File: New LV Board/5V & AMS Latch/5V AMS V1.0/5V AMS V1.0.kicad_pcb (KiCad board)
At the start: 2 copper layers, 46.4 x 64.5 mm, 19 parts, among them J2 B12B-PH-K-S, J4 691137710002, J6 PH1-20-UA, J9 PH1-20-UA, K1 AHES4291, SW1 Test Reset AMS, U1 LT1117-5.0

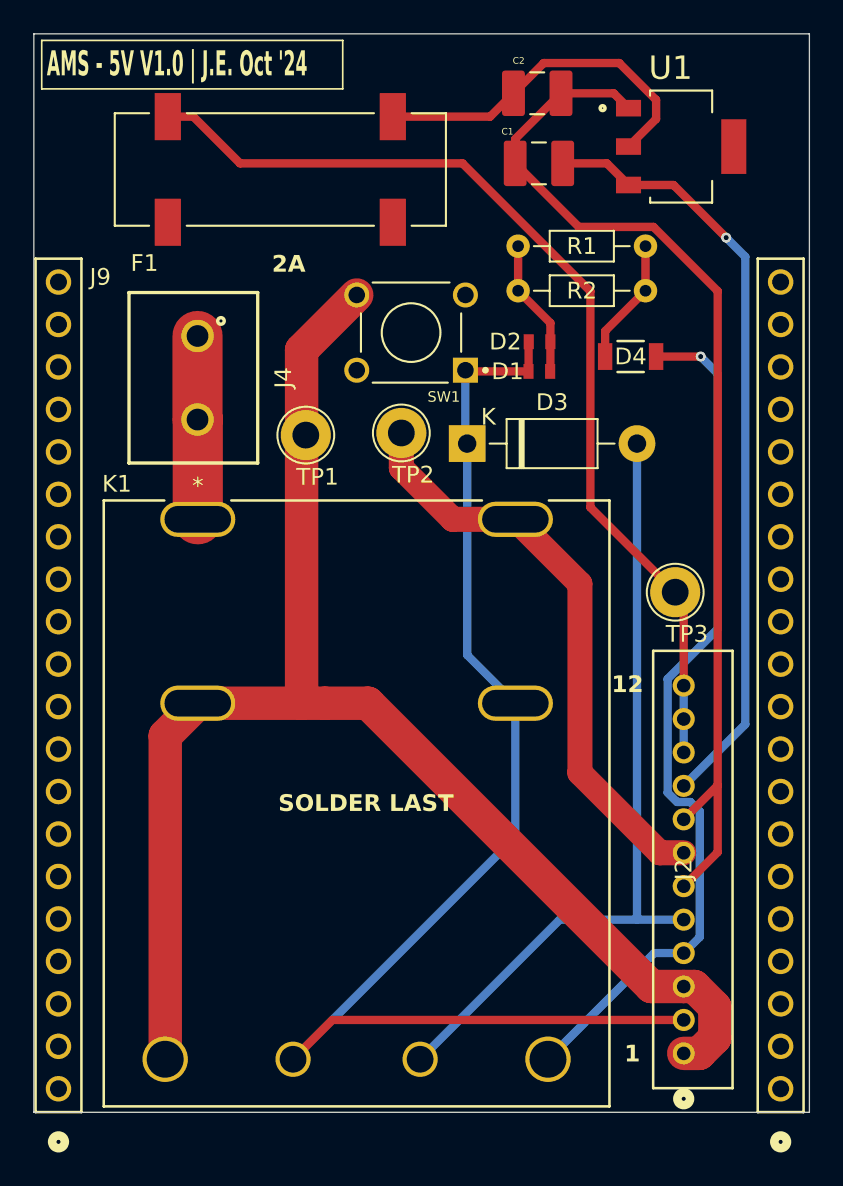
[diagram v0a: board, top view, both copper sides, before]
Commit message: getting dimensions correct for 5V AMS
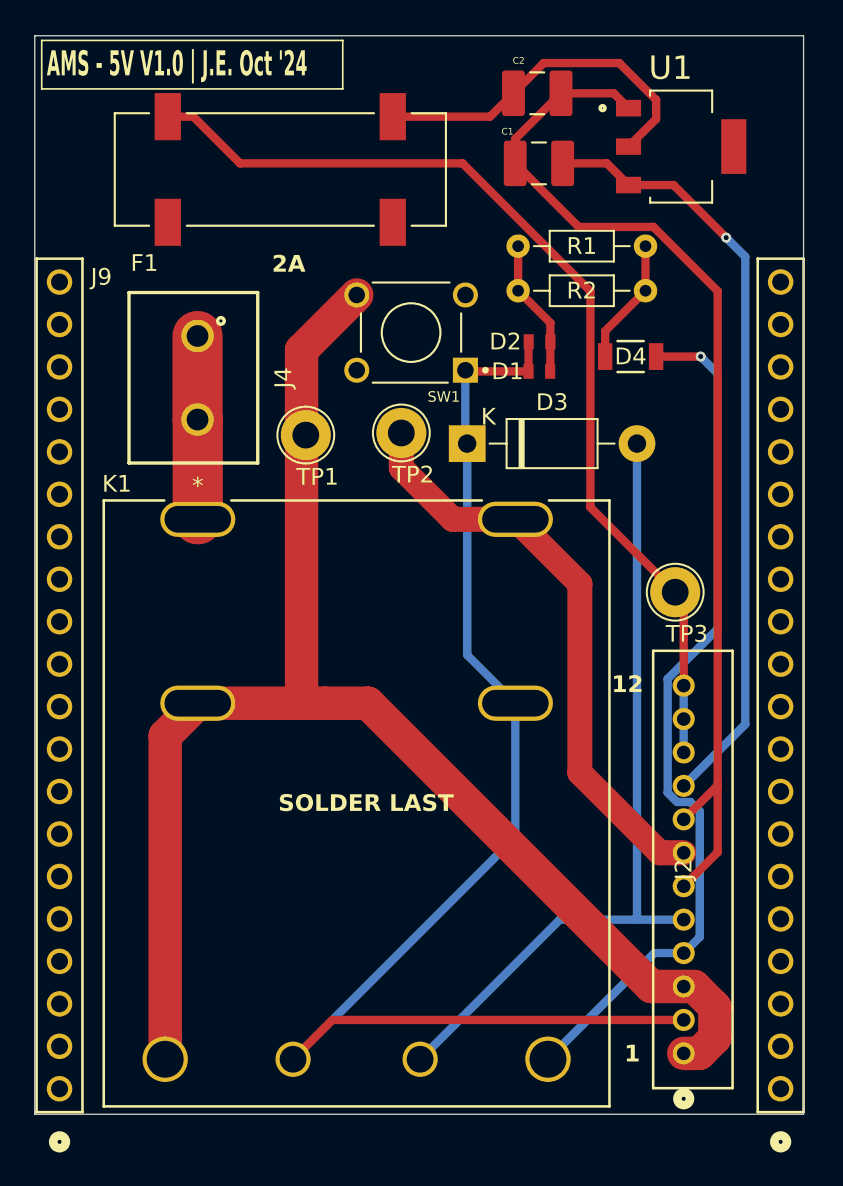
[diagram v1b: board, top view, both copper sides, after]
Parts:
- moved J9 0.06 mm to (59.9, 168.6)
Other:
- board size 46.4 x 64.5 mm -> 46 x 64.5 mm
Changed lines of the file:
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@@
 	(footprint "PH1-20-UA:CONN_PH1-20-UA_ADM"
 		(layer "F.Cu")
-		(at 59.881 168.643 90)
+		(at 59.944 168.643 90)
 		(tags "PH1-20-UA ")
 		(property "Reference" "J9"
@@
 	)
 	(gr_rect
-		(start 58.407 105.537)
-		(end 104.801 170.053)
+		(start 58.464 105.651)
+		(end 104.4516 170.167)
 		(stroke
 			(width 0.05)
@@
 		)
 	)
+	(dimension
+		(type orthogonal)
+		(layer "Dwgs.User")
+		(pts
+			(xy 104.4516 105.651) (xy 104.4516 170.167)
+		)
+		(height 5.2002)
+		(orientation 1)
+		(format
+			(prefix "")
+			(suffix "mm")
+			(units 3)
+			(units_format 0)
+			(precision 4)
+			(suppress_zeroes yes)
+		)
+		(style
+			(thickness 0.2)
+			(arrow_length 1.27)
+			(text_position_mode 0)
+			(arrow_direction outward)
+			(extension_height 0.58642)
+			(extension_offset 0.5)
+		)
+		(gr_text "64.516mm"
+			(at 107.8518 137.909 90)
+			(layer "Dwgs.User")
+			(effects
+				(font
+					(size 1.5 1.5)
+					(thickness 0.3)
+				)
+			)
+		)
+	)
+	(dimension
+		(type orthogonal)
+		(layer "Dwgs.User")
+		(pts
+			(xy 58.4708 169.418) (xy 104.4708 169.418)
+		)
+		(height 15.748)
+		(orientation 0)
+		(format
+			(prefix "")
+			(suffix "")
+			(units 3)
+			(units_format 1)
+			(precision 4)
+		)
+		(style
+			(thickness 0.05)
+			(arrow_length 1.27)
+			(text_position_mode 0)
+			(arrow_direction outward)
+			(extension_height 0.58642)
+			(extension_offset 0.5)
+			(keep_text_aligned yes)
+		)
+		(gr_text "46.0000 mm"
+			(at 81.4708 184.016 0)
+			(layer "Dwgs.User")
+			(effects
+				(font
+					(size 1 1)
+					(thickness 0.15)
+				)
+			)
+		)
+	)
+	(dimension
+		(type orthogonal)
+		(layer "Dwgs.User")
+		(pts
+			(xy 103.124 168.275) (xy 59.944 168.275)
+		)
+		(height 9.144)
+		(orientation 0)
+		(format
+			(prefix "")
+			(suffix "")
+			(units 3)
+			(units_format 1)
+			(precision 4)
+		)
+		(style
+			(thickness 0.05)
+			(arrow_length 1.27)
+			(text_position_mode 0)
+			(arrow_direction outward)
+			(extension_height 0.58642)
+			(extension_offset 0.5)
+			(keep_text_aligned yes)
+		)
+		(gr_text "43.1800 mm"
+			(at 81.534 176.269 0)
+			(layer "Dwgs.User")
+			(effects
+				(font
+					(size 1 1)
+					(thickness 0.15)
+				)
+			)
+		)
+	)

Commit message: PCB cleanup and retrace
PCB cleanup and retrace
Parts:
- removed K1: AHES4291, motorSports:AHES4_PAN
- removed TP1, TP2, TP3: TestPoint, TestPoint:TestPoint_Loop_D2.60mm_Drill1.6mm_Beaded
- added K2: A161CS12VDC.64, Footprints:RELAY_A161CS12VDC.64, F.Cu at (76.5, 140.9)
- added K3: A161CS12VDC.64, Footprints:RELAY_A161CS12VDC.64, F.Cu at (76.5, 150.0)
- added K4: A161CS12VDC.64, Footprints:RELAY_A161CS12VDC.64, F.Cu at (76.5, 159.1)
- J2: footprint MotorSports_KICad:CONN12_B12B-PH_JST -> Footprints:JST_B12B-PH-K-S
- moved F1 35.5 mm to (94.8, 141.8), turned to 90 degrees
- moved R1 34.3 mm to (86.0, 152.5), turned to 90 degrees
- moved D2 33.1 mm to (89.4, 157.0)
- moved D3 30.7 mm to (88.3, 160.5)
- moved D4 29.7 mm to (95.0, 154.5)
- moved D1 28.8 mm to (89.4, 154.5)
- moved R2 19.3 mm to (86.0, 140.1), turned to 90 degrees
- moved C2 18.0 mm to (86.6, 127.0)
- moved J2 14.8 mm to (82.5, 166.6), turned to 180 degrees
- moved U1 12.3 mm to (96.0, 124.5)
- moved C1 8.95 mm to (86.6, 122.0)
- moved SW1 6.72 mm to (78.8, 129.8)
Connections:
- D3 pad 2: Net-(D3-A) -> Net-(D1-K)
- J2 pad 5: Net-(D3-A) -> Net-(D1-K)
- SW1 pad 2: (no net) -> Net-(J2-Pad1)
- SW1 pad 4: Net-(J2-Pad1) -> (no net)
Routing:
- net Net-(J2-Pad1): track 90.4 -> 41.9 mm
- net Net-(D3-A): track 47.7 -> 0.00 mm
- net Net-(F1-Pad1_1): track 59.7 -> 23.8 mm
- net Net-(J2-Pad7): track 35.1 -> 4.92 mm
- net Net-(D4-K): track 7.60 -> 33.0 mm, vias 0 -> 1
- net Net-(J4-Pad1): track 11.0 -> 36.4 mm
- net Net-(D1-K): track 77.9 -> 73.4 mm
- net /GND: track 72.6 -> 68.3 mm
- net Net-(U1-VO): track 21.5 -> 24.6 mm, vias 0 -> 2
- net /Vs: track 46.4 -> 49.3 mm, vias 1 -> 0
- net Net-(D4-A): track 52.4 -> 52.2 mm, vias 1 -> 2
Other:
- board size 46 x 64.5 mm -> 46 x 51.5 mm
- board text added: "AMS - 5V V1.0 | H.R. Nov 13' 2025"
- board text removed: "AMS - 5V V1.0 | J.E. Oct '24"

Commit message: cleaned up schematics
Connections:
- D2 pad 1: Net-(D1-K) -> Net-(D2-K)
- D3 pad 1: Net-(D1-K) -> Net-(D2-K)
- D3 pad 2: Net-(D1-K) -> Net-(D3-A)
- J2 pad 2: Net-(D1-K) -> Net-(D2-K)
- J2 pad 5: Net-(D1-K) -> Net-(D3-A)
- K2 pad A1: Net-(D1-K) -> Net-(D3-A)
- K2 pad A2: Net-(D1-K) -> Net-(D2-K)
- K3 pad A1: Net-(D1-K) -> Net-(D3-A)
- K3 pad A2: Net-(D1-K) -> Net-(D2-K)
- K3 pad NO: Net-(D1-K) -> Net-(D2-K)
- K4 pad A1: Net-(D1-K) -> Net-(D2-K)
- SW1 pad 1: Net-(D1-K) -> Net-(D2-K)
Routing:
- net Net-(D1-K): track 73.4 -> 55.2 mm
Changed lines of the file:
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@@
 	(net 27 "unconnected-(K3-PadNC)")
 	(net 28 "unconnected-(K4-PadNC)")
+	(net 29 "Net-(D2-K)")
+	(net 30 "Net-(D3-A)")
 	(footprint "motorSports:CAPC3225X270N"
 		(layer "F.Cu")
@@
 			)
 		)
-		(property "Datasheet" "~"
+		(property "Datasheet" ""
 			(at 0 0 0)
 			(layer "F.Fab")
@@
 			)
 		)
-		(property "Datasheet" "~"
+		(property "Datasheet" ""
 			(at 0 0 0)
 			(layer "F.Fab")
@@
 			(layers "*.Cu" "*.Mask")
 			(remove_unused_layers no)
-			(net 4 "Net-(D1-K)")
+			(net 29 "Net-(D2-K)")
 			(pinfunction "K")
 			(pintype "passive")
@@
 			(layers "*.Cu" "*.Mask")
 			(remove_unused_layers no)
-			(net 4 "Net-(D1-K)")
+			(net 30 "Net-(D3-A)")
 			(pinfunction "A")
 			(pintype "passive")
@@
 			)
 		)
-		(property "Datasheet" "~"
+		(property "Datasheet" ""
 			(at 0 0 90)
 			(unlocked yes)
@@
 			(layers "*.Cu" "*.Mask")
 			(remove_unused_layers no)
-			(net 4 "Net-(D1-K)")
+			(net 29 "Net-(D2-K)")
 			(pintype "passive")
 			(solder_mask_margin 0.102)
@@
 			(layers "*.Cu" "*.Mask")
 			(remove_unused_layers no)
-			(net 4 "Net-(D1-K)")
+			(net 30 "Net-(D3-A)")
 			(pintype "passive")
 			(solder_mask_margin 0.102)
@@
 			(layers "*.Cu" "*.Mask")
 			(remove_unused_layers no)
-			(net 4 "Net-(D1-K)")
+			(net 29 "Net-(D2-K)")
 			(pintype "passive")
 			(solder_mask_margin 0.102)
@@
 			(layers "*.Cu" "*.Mask")
 			(remove_unused_layers no)
-			(net 4 "Net-(D1-K)")
+			(net 29 "Net-(D2-K)")
 			(pinfunction "2")
 			(pintype "unspecified")
@@
 			(layers "*.Cu" "*.Mask")
 			(remove_unused_layers no)
-			(net 4 "Net-(D1-K)")
+			(net 30 "Net-(D3-A)")
 			(pinfunction "5")
 			(pintype "unspecified")
@@
 			)
 		)
-		(property "Datasheet" "~"
+		(property "Datasheet" ""
 			(at 0 0 0)
 			(layer "F.Fab")
@@
 			)
 		)
-		(property "Datasheet" "~"
+		(property "Datasheet" ""
 			(at 0 0 0)
 			(layer "F.Fab")
@@
 			(size 0.6096 0.889)
 			(layers "F.Cu" "F.Mask" "F.Paste")
-			(net 4 "Net-(D1-K)")
+			(net 29 "Net-(D2-K)")
 			(pinfunction "K")
 			(pintype "passive")
@@
 			)
 		)
-		(property "Datasheet" "~"
+		(property "Datasheet" ""
 			(at 0 0 0)
 			(layer "F.Fab")
@@
 			)
 		)
-		(property "Datasheet" "~"
+		(property "Datasheet" ""
 			(at 0 0 90)
 			(unlocked yes)
@@
 			)
 		)
-		(property "Datasheet" "~"
+		(property "Datasheet" ""
 			(at 0 0 0)
 			(layer "F.Fab")
@@
 			(layers "*.Cu" "*.Mask")
 			(remove_unused_layers no)
-			(net 4 "Net-(D1-K)")
+			(net 29 "Net-(D2-K)")
 			(pinfunction "1")
 			(pintype "passive")
@@
 			(layers "*.Cu" "*.Mask")
 			(remove_unused_layers no)
-			(net 4 "Net-(D1-K)")
+			(net 30 "Net-(D3-A)")
 			(pintype "passive")
 			(solder_mask_margin 0.102)
@@
 			(layers "*.Cu" "*.Mask")
 			(remove_unused_layers no)
-			(net 4 "Net-(D1-K)")
+			(net 29 "Net-(D2-K)")
 			(pintype "passive")
 			(solder_mask_margin 0.102)
@@
 			(layers "*.Cu" "*.Mask")
 			(remove_unused_layers no)
-			(net 4 "Net-(D1-K)")
+			(net 29 "Net-(D2-K)")
 			(pintype "passive")
 			(solder_mask_margin 0.102)
@@
 	)
 	(segment
-		(start 78.58 143.255)
-		(end 78.58 147.625)
-		(width 0.2)
-		(layer "F.Cu")
-		(net 4)
-	)
-	(segment
 		(start 78.58 152.375)
 		(end 78.58 147.625)
@@
 		(width 0.2)
 		(layer "F.Cu")
-		(net 4)
-	)
-	(segment
-		(start 78.58 161.495)
-		(end 78.58 156.745)
-		(width 0.2)
-		(layer "F.Cu")
-		(net 4)
-	)
-	(segment
-		(start 78.58 152.375)
-		(end 78.58 156.745)
-		(width 0.2)
-		(layer "F.Cu")
-		(net 4)
-	)
-	(segment
-		(start 78.58 138.505)
-		(end 78.58 143.255)
-		(width 0.2)
-		(layer "F.Cu")
